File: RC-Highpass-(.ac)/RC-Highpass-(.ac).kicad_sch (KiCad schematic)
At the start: 3 parts

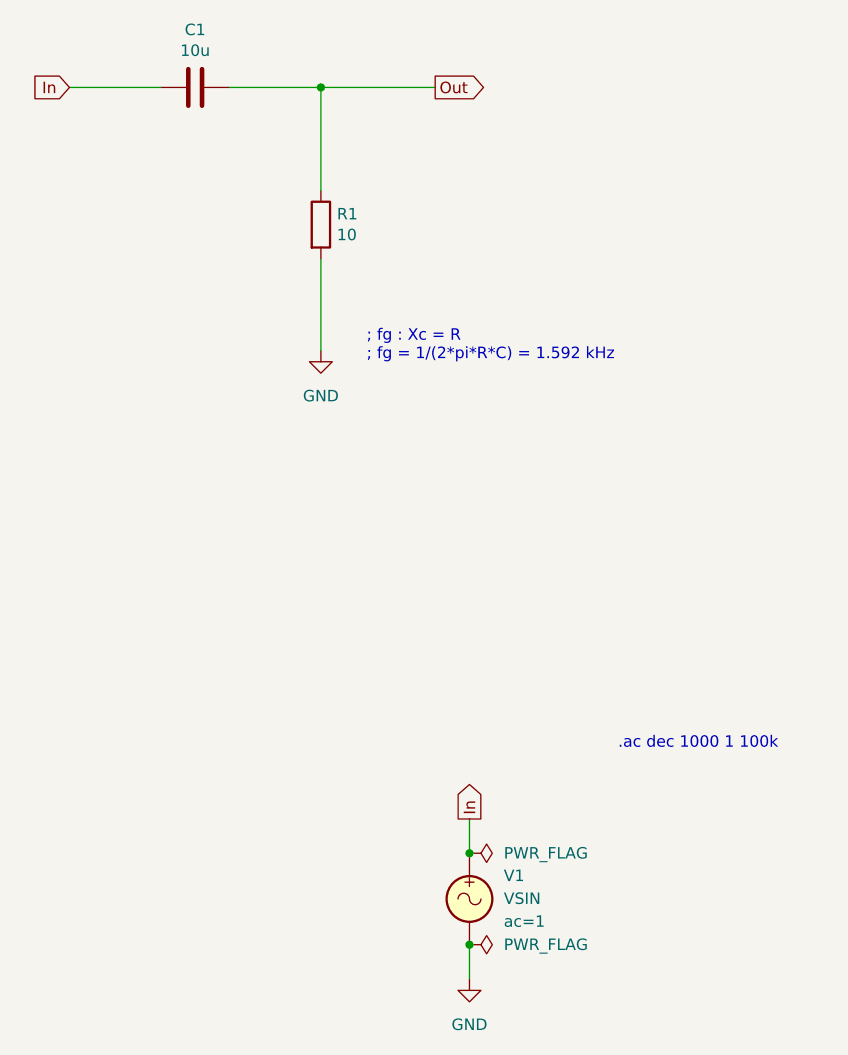
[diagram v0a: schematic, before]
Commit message: Updated all schematics and prepared for KiCad 8.0
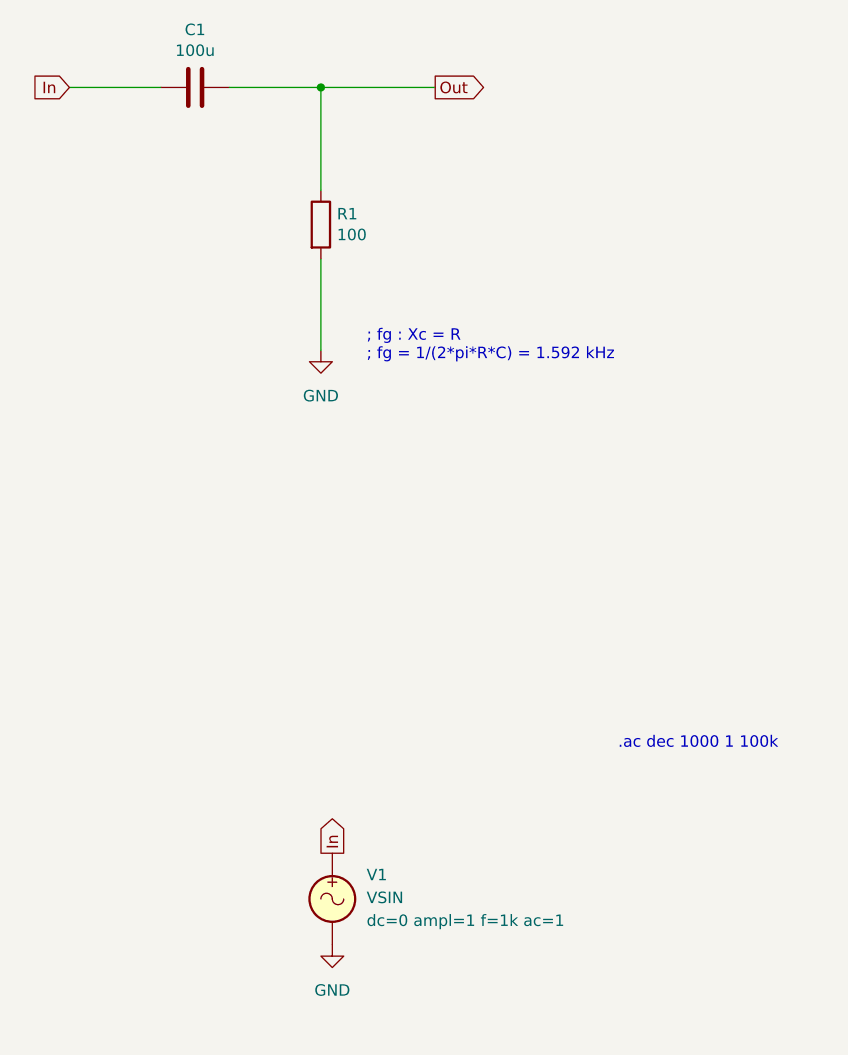
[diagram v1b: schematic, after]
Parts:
- C1: value 10u -> 100u
- R1: value 10 -> 100
